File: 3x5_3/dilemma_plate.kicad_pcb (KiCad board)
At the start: 2 copper layers, 115.5 x 95.2 mm, 22 parts, among them SW101 NA_SW_Push, SW102 NA_SW_Push, SW103 NA_SW_Push, SW104 NA_SW_Push, SW105 NA_SW_Push, SW106 NA_SW_Push, SW107 NA_SW_Push, SW108 NA_SW_Push, SW109 NA_SW_Push, SW112 NA_SW_Push, SW113 NA_SW_Push, SW114 NA_SW_Push, SW115 NA_SW_Push, SW116 NA_SW_Push, SW117 NA_SW_Push, SW118 NA_SW_Push, SW119 NA_SW_Push, SW3001 NA_SW_Push

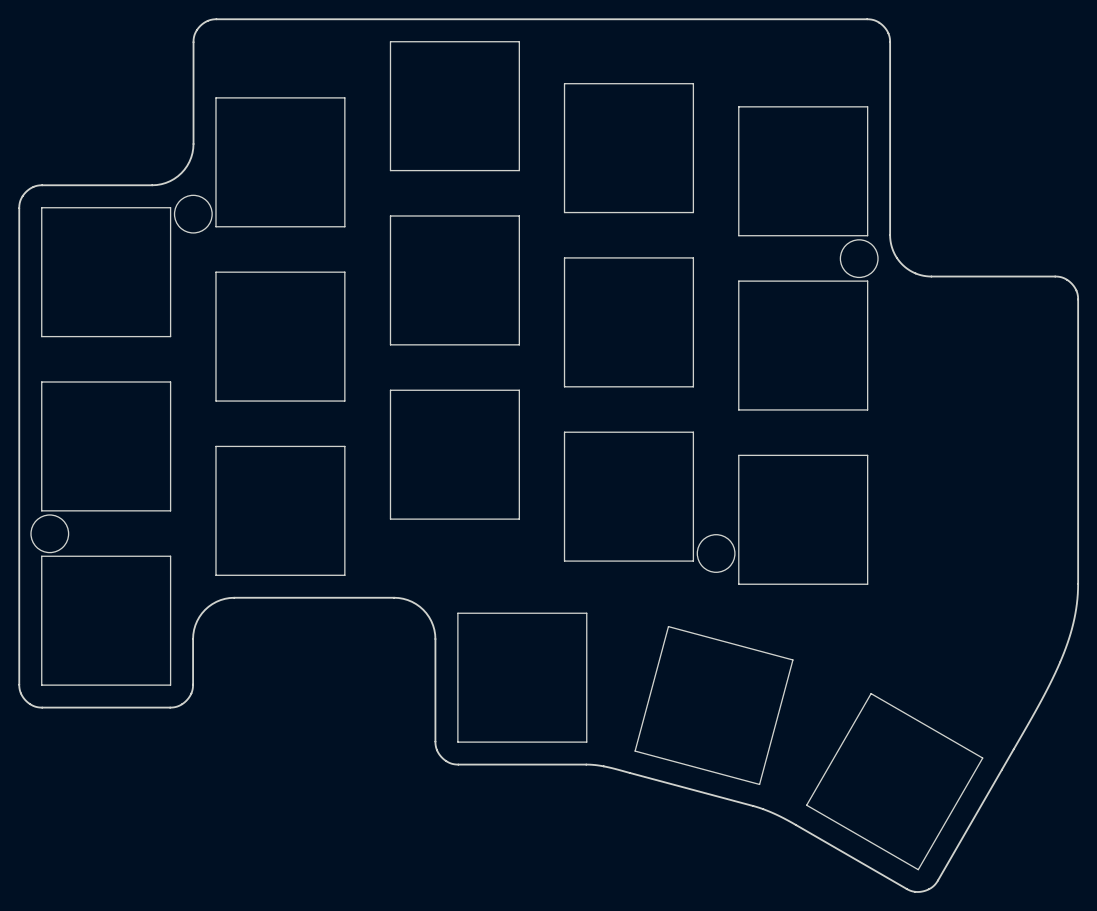
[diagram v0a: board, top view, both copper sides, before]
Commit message: adjust nicenano .gitignore & fix on/off silkscreen
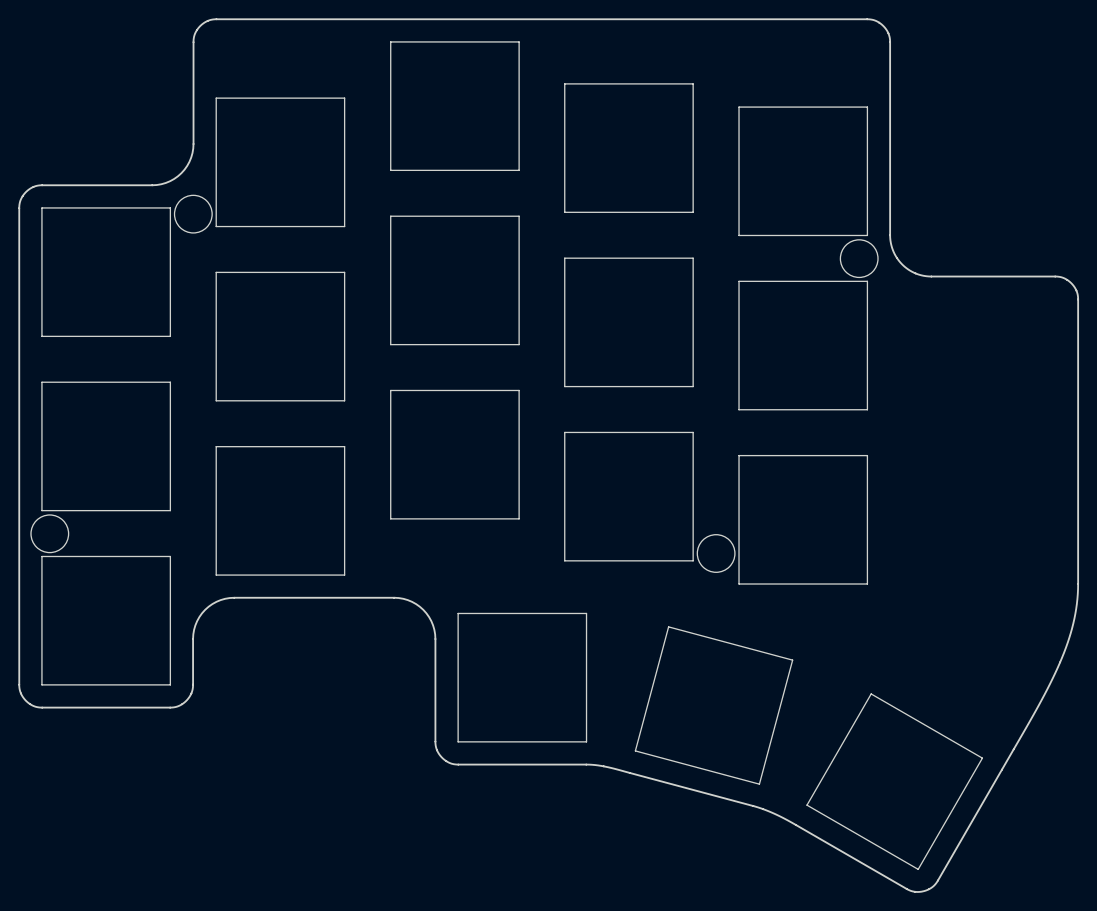
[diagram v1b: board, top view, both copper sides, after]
